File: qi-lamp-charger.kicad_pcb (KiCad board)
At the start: 2 copper layers, 41.5 x 44 mm, 85 parts, among them J1 Conn_01x03, J2 Conn_01x02, J4 Conn_01x06, J5 Conn_01x03, Q1 BSS308PE H6327, SW1 SKTDLDE010, U1 SLG5NV1430V, U2 BQ51050BRHL, U3 ESP-12E

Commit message: Shematic changed
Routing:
- net LED_V+: track 160.8 -> 159.8 mm
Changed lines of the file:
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@@
   (via (at 90.4 104.2) (size 0.8) (drill 0.4) (layers "F.Cu" "B.Cu") (net 5))
   (via (at 92.1 112) (size 0.8) (drill 0.4) (layers "F.Cu" "B.Cu") (net 5))
-  (via (at 96.3 105.5) (size 0.8) (drill 0.4) (layers "F.Cu" "B.Cu") (net 5))
+  (via (at 96.6 105.3) (size 0.8) (drill 0.4) (layers "F.Cu" "B.Cu") (net 5))
   (via (at 81.5 92.1) (size 0.8) (drill 0.4) (layers "F.Cu" "B.Cu") (net 5))
   (via (at 97.6 116.9) (size 0.8) (drill 0.4) (layers "F.Cu" "B.Cu") (net 5))
@@
   (segment (start 90.974999 110.3) (end 90.975 109.625) (width 0.35) (layer "B.Cu") (net 15))
   (segment (start 90.325 107.375) (end 90.3 107.35) (width 0.5) (layer "B.Cu") (net 15))
+  (segment (start 95.875489 107.224511) (end 95.5 107.6) (width 0.25) (layer "B.Cu") (net 15))
   (segment (start 81.4 103.1) (end 81.2 102.9) (width 0.25) (layer "B.Cu") (net 15))
   (segment (start 103.325 89.4) (end 103.125 89.6) (width 0.25) (layer "B.Cu") (net 15))
@@
   (segment (start 82.1 110.4) (end 81.4 109.7) (width 0.25) (layer "B.Cu") (net 15))
   (segment (start 88.1 109.2) (end 89.95 107.35) (width 0.5) (layer "B.Cu") (net 15))
+  (segment (start 98.85 101.05) (end 95.875489 104.024511) (width 0.25) (layer "B.Cu") (net 15))
   (segment (start 107.700978 110.2) (end 107.875 110.2) (width 0.25) (layer "B.Cu") (net 15))
   (segment (start 91.3 107.4) (end 91.325 107.375) (width 0.5) (layer "B.Cu") (net 15))
-  (segment (start 95.5 104.4) (end 95.5 105.9) (width 0.25) (layer "B.Cu") (net 15))
   (segment (start 103.2 105.4) (end 98.85 101.05) (width 0.25) (layer "B.Cu") (net 15))
   (segment (start 95.275 107.375) (end 95.5 107.6) (width 0.5) (layer "B.Cu") (net 15))
@@
   (segment (start 102.1 87) (end 102 86.9) (width 0.25) (layer "B.Cu") (net 15))
   (segment (start 104.5 89.4) (end 104.5 95.4) (width 0.25) (layer "B.Cu") (net 15))
-  (segment (start 98.85 101.05) (end 95.5 104.4) (width 0.25) (layer "B.Cu") (net 15))
+  (segment (start 95.875489 104.024511) (end 95.875489 107.224511) (width 0.25) (layer "B.Cu") (net 15))
   (segment (start 106.5 106.1) (end 105.8 105.4) (width 0.25) (layer "B.Cu") (net 15))
-  (segment (start 95.5 105.9) (end 95.5 107.6) (width 0.25) (layer "B.Cu") (net 15))
   (segment (start 112.870636 90.937083) (end 114.397432 90.937083) (width 0.25) (layer "F.Cu") (net 16))
   (segment (start 112.1 85.2) (end 112.1 90.166447) (width 0.25) (layer "F.Cu") (net 16))
@@
   (segment (start 106.4 104.375) (end 106.425 104.4) (width 0.5) (layer "F.Cu") (net 23))
   (segment (start 104.4 93.625) (end 104.625 93.625) (width 0.5) (layer "F.Cu") (net 23))
-  (segment (start 93.5 100) (end 94.8 101.3) (width 0.5) (layer "F.Cu") (net 23))
   (segment (start 112.111791 109.821762) (end 111.933553 110) (width 0.5) (layer "F.Cu") (net 23))
+  (segment (start 94.8 101.775) (end 97.6 104.575) (width 0.5) (layer "F.Cu") (net 23))
   (segment (start 110.698609 110) (end 106.425 105.726391) (width 0.5) (layer "F.Cu") (net 23))
   (segment (start 86.4 107.5) (end 85.438209 106.538209) (width 0.5) (layer "F.Cu") (net 23))
   (segment (start 106.4 104.375) (end 106.375 104.4) (width 0.5) (layer "F.Cu") (net 23))
   (segment (start 85.438209 106.538209) (end 85.438209 105.578238) (width 0.5) (layer "F.Cu") (net 23))
-  (segment (start 94.8 101.3) (end 94.8 103.5) (width 0.5) (layer "F.Cu") (net 23))
   (segment (start 99.925 104.575) (end 103.449999 101.050001) (width 0.5) (layer "F.Cu") (net 23))
-  (segment (start 93.6 97.55) (end 93.5 97.65) (width 0.5) (layer "F.Cu") (net 23))
   (segment (start 95.625 115.4) (end 95.5 115.525) (width 0.5) (layer "F.Cu") (net 23))
   (segment (start 83.859394 110.859394) (end 82.4 109.4) (width 0.5) (layer "F.Cu") (net 23))
@@
   (segment (start 87.888209 90.178238) (end 87.888209 89.270461) (width 0.5) (layer "F.Cu") (net 23))
   (segment (start 105 101.050001) (end 106.4 102.450001) (width 0.5) (layer "F.Cu") (net 23))
-  (segment (start 94.8 103.5) (end 95.875 104.575) (width 0.5) (layer "F.Cu") (net 23))
+  (segment (start 93.6 97.55) (end 93.5 97.65) (width 0.5) (layer "F.Cu") (net 23))
   (segment (start 97.55 104.625) (end 97.6 104.575) (width 0.5) (layer "F.Cu") (net 23))
   (segment (start 92.9 86.7) (end 94.5 88.3) (width 0.5) (layer "F.Cu") (net 23))
@@
   (segment (start 93.575 115.525) (end 95.5 115.525) (width 0.5) (layer "F.Cu") (net 23))
   (segment (start 91.6 86.7) (end 92.9 86.7) (width 0.5) (layer "F.Cu") (net 23))
+  (segment (start 93.5 100) (end 94.8 101.3) (width 0.5) (layer "F.Cu") (net 23))
   (segment (start 91.3 117.8) (end 93.575 115.525) (width 0.5) (layer "F.Cu") (net 23))
   (segment (start 88.55 116.4) (end 89.95 117.8) (width 0.5) (layer "F.Cu") (net 23))
+  (segment (start 93.5 97.65) (end 93.5 100) (width 0.5) (layer "F.Cu") (net 23))
   (segment (start 87.3 116) (end 83.859394 112.559394) (width 0.5) (layer "F.Cu") (net 23))
   (segment (start 90.0125 88.2875) (end 91.6 86.7) (width 0.5) (layer "F.Cu") (net 23))
@@
   (segment (start 95.475 115.525) (end 95.5 115.525) (width 0.5) (layer "F.Cu") (net 23))
   (segment (start 88.87117 88.2875) (end 90.0125 88.2875) (width 0.5) (layer "F.Cu") (net 23))
+  (segment (start 94.8 101.3) (end 94.8 101.775) (width 0.5) (layer "F.Cu") (net 23))
   (segment (start 102.45 84.6) (end 104.375 84.6) (width 0.5) (layer "F.Cu") (net 23))
   (segment (start 109.875 89.734971) (end 109.875 89.425) (width 0.25) (layer "F.Cu") (net 23))
   (segment (start 103.449999 101.050001) (end 105 101.050001) (width 0.5) (layer "F.Cu") (net 23))
-  (segment (start 93.5 97.65) (end 93.5 100) (width 0.5) (layer "F.Cu") (net 23))
-  (segment (start 95.875 104.575) (end 97.6 104.575) (width 0.5) (layer "F.Cu") (net 23))
   (segment (start 106.425 105.726391) (end 106.425 104.4) (width 0.5) (layer "F.Cu") (net 23))
   (segment (start 104.375 84.6) (end 104.4 84.625) (width 0.5) (layer "F.Cu") (net 23))
@@
   (segment (start 103.5 104.8) (end 108.2 104.8) (width 0.25) (layer "B.Cu") (net 48))
   (segment (start 89.2 97.334643) (end 89.2 97.8) (width 0.25) (layer "F.Cu") (net 49))
+  (segment (start 91.8 103.1) (end 91.8 103.2) (width 0.25) (layer "F.Cu") (net 49))
+  (segment (start 87 95.5) (end 87.365357 95.5) (width 0.25) (layer "F.Cu") (net 49))
   (segment (start 94 105.4) (end 94 109.1) (width 0.25) (layer "F.Cu") (net 49))
-  (segment (start 87 95.5) (end 87.365357 95.5) (width 0.25) (layer "F.Cu") (net 49))
   (segment (start 91.8 103.2) (end 94 105.4) (width 0.25) (layer "F.Cu") (net 49))
   (segment (start 87.365357 95.5) (end 89.2 97.334643) (width 0.25) (layer "F.Cu") (net 49))
@@
   (via (at 89.2 97.8) (size 0.8) (drill 0.4) (layers "F.Cu" "B.Cu") (net 49))
   (via (at 94 109.1) (size 0.8) (drill 0.4) (layers "F.Cu" "B.Cu") (net 49))
-  (via (at 91.8 103.2) (size 0.8) (drill 0.4) (layers "F.Cu" "B.Cu") (net 49))
+  (via (at 91.8 103.1) (size 0.8) (drill 0.4) (layers "F.Cu" "B.Cu") (net 49))
   (via (at 87 95.5) (size 0.8) (drill 0.4) (layers "F.Cu" "B.Cu") (net 49))
+  (segment (start 91.8 102.1) (end 92.9 101) (width 0.25) (layer "B.Cu") (net 49))
   (segment (start 95.2 96) (end 94.1 96) (width 0.25) (layer "B.Cu") (net 49))
   (segment (start 91.6 96) (end 91 96.6) (width 0.25) (layer "B.Cu") (net 49))
@@
   (segment (start 94 109.1) (end 94 111.5) (width 0.2) (layer "B.Cu") (net 49))
   (segment (start 94.1 96) (end 91.6 96) (width 0.25) (layer "B.Cu") (net 49))
+  (segment (start 92.9 101) (end 94 101) (width 0.25) (layer "B.Cu") (net 49))
   (segment (start 83.925001 95.5) (end 83.300002 96.124999) (width 0.25) (layer "B.Cu") (net 49))
   (segment (start 87 95.5) (end 83.925001 95.5) (width 0.25) (layer "B.Cu") (net 49))
@@
   (segment (start 96.6 97.4) (end 95.2 96) (width 0.25) (layer "B.Cu") (net 49))
   (segment (start 89.8 97.8) (end 89.2 97.8) (width 0.25) (layer "B.Cu") (net 49))
-  (segment (start 91.8 102.1) (end 92.9 101) (width 0.25) (layer "B.Cu") (net 49))
-  (segment (start 92.9 101) (end 94 101) (width 0.25) (layer "B.Cu") (net 49))
   (segment (start 91 96.6) (end 89.8 97.8) (width 0.25) (layer "B.Cu") (net 49))
   (segment (start 95.6 101) (end 97.9 98.7) (width 0.25) (layer "B.Cu") (net 49))
   (segment (start 95.05 112.55) (end 96.349998 112.55) (width 0.2) (layer "B.Cu") (net 49))
-  (segment (start 91.8 103.2) (end 91.8 102.1) (width 0.25) (layer "B.Cu") (net 49))
+  (segment (start 91.8 103.1) (end 91.8 102.1) (width 0.25) (layer "B.Cu") (net 49))
   (segment (start 95.6 98.6) (end 95.6 98.9) (width 0.25) (layer "F.Cu") (net 51))
   (segment (start 95.6 98.9) (end 98.9 102.2) (width 0.25) (layer "F.Cu") (net 51))

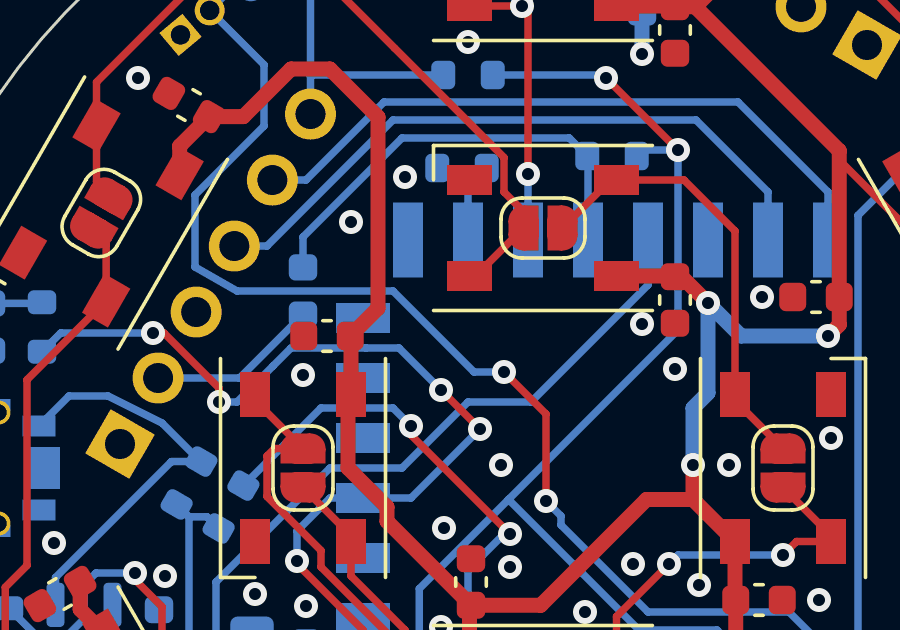
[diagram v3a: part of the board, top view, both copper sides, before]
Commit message: Minor corrections to layout (not up to date with previous commit)
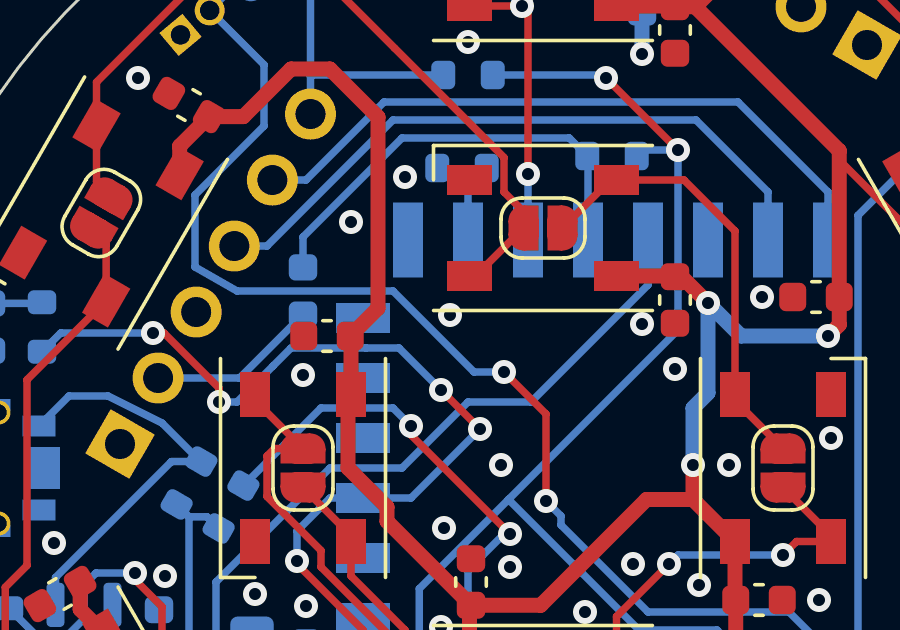
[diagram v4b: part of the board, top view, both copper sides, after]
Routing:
- net GND: vias 40 -> 41
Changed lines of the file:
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@@
   (via (at 90.4 104.2) (size 0.8) (drill 0.4) (layers "F.Cu" "B.Cu") (net 5))
   (via (at 92.1 112) (size 0.8) (drill 0.4) (layers "F.Cu" "B.Cu") (net 5))
+  (via (at 96.9 94.9) (size 0.8) (drill 0.4) (layers "F.Cu" "B.Cu") (net 5))
   (via (at 96.6 105.3) (size 0.8) (drill 0.4) (layers "F.Cu" "B.Cu") (net 5))
   (via (at 81.5 92.1) (size 0.8) (drill 0.4) (layers "F.Cu" "B.Cu") (net 5))

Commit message: Puzzle #6
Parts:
- removed H1, H2, H3: MountingHole, MountingHole:MountingHole_3.2mm_M3_ISO14580
- removed JP12: SolderJumper_2_Bridged, Jumper:SolderJumper-2_P1.3mm_Bridged_RoundedPad1.0x1.5mm
- added D13: CD0603-B0340R, Diode_SMD:D_0603_1608Metric, B.Cu at (64.2, 82.2)
- added R15: 20k, Resistor_SMD:R_0603_1608Metric, B.Cu at (56.1, 79.6)
- added R16: 20k, Resistor_SMD:R_0603_1608Metric, F.Cu at (82.5, 96.0)
- added R17: 340k, Resistor_SMD:R_0603_1608Metric, B.Cu at (60.1, 82.1)
- added R18: 100k, Resistor_SMD:R_0603_1608Metric, B.Cu at (56.1, 82.1)
- moved D12 31.4 mm to (64.2, 79.6), turned to 180 degrees
- moved TP1 0.89 mm to (88.7, 85.2), turned to 130 degrees
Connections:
- net PWR_ON/~{OFF} renamed KEEP_ALIVE
- D12 pad 1: DTR -> ~{Qi_CHG/LED}
- D12 pad 2: ESP_GPIO0 -> Net-(Q1-Pad1)
- Q1 pad 1: BTN -> Net-(Q1-Pad1)
- R11 pad 1: ESP_GPIO0 -> DTR
- R14 pad 1: BTN -> Net-(Q1-Pad1)
- R4 pad 1: ~{Qi_CHG/LED} -> Net-(R4-Pad1)
- SW1 pad 2: BTN -> ~{BTN}
- TP1 pad 2: ~{ESP_RST} -> DTR
- U2 pad 7: ~{Qi_CHG/LED} -> Net-(R4-Pad1)
- U3 pad 1: ~{ESP_RST} -> RTS
- U3 pad 18: ESP_GPIO0 -> DTR
- U3 pad 2: NTC -> BAT_ADC
- U3 pad 20: unconnected-(U3-Pad20) -> Qi_TS/CTRL
- U3 pad 5: BTN -> ~{BTN}
- U3 pad 7: Qi_TS/CTRL -> unconnected-(U3-Pad7)
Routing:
- net GND: track 38.0 -> 87.0 mm, vias 41 -> 48
- net ~{ESP_RST}: track 41.7 -> 0.00 mm, vias 2 -> 0
- net ~{Qi_CHG/LED}: track 38.6 -> 0.00 mm, vias 6 -> 0
- net RTS: track 9.98 -> 40.8 mm, vias 0 -> 2
- net ~{BTN}: track 0.00 -> 29.4 mm, vias 0 -> 4
- net DTR: track 5.71 -> 32.3 mm, vias 0 -> 1
- net Net-(R4-Pad1): track 0.00 -> 25.1 mm, vias 0 -> 2
- net ESP_GPIO0: track 14.9 -> 0.00 mm
- net BAT_ADC: track 0.00 -> 14.8 mm, vias 0 -> 1
- net BTN: track 13.9 -> 0.00 mm
- net Net-(Q1-Pad1): track 0.00 -> 7.38 mm
- net NTC: track 40.0 -> 33.0 mm
- net LED_DOUT: track 22.4 -> 18.7 mm
- net Qi_TS/CTRL: track 45.4 -> 49.0 mm, vias 2 -> 3
- net +VSW: track 77.9 -> 79.5 mm
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
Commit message: Puzzle #7
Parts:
- moved R15 33.6 mm to (88.5, 88.5), turned to 135 degrees
- moved R18 29.7 mm to (85.2, 88.0), turned to -130 degrees
- moved R17 25.3 mm to (83.3, 92.3), turned to -90 degrees
- moved D12 25.3 mm to (87.4, 89.6), turned to 135 degrees
- moved D13 23.7 mm to (86.0, 91.5), turned to 0 degrees
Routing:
- net GND: track 87.0 -> 239.0 mm, vias 48 -> 52
- net BAT_ADC: track 14.8 -> 47.5 mm, vias 1 -> 2
- net ~{Qi_CHG/LED}: track 0.00 -> 18.6 mm, vias 0 -> 2
- net Net-(D12-Pad2): track 7.38 -> 18.9 mm
- net Net-(R15-Pad2): track 25.1 -> 35.1 mm
- net ~{BTN}: track 29.4 -> 36.4 mm, vias 4 -> 5
- net +VSW: track 79.5 -> 84.8 mm
- net DTR: track 32.3 -> 33.4 mm
- net LED_V+: track 160.8 -> 159.7 mm

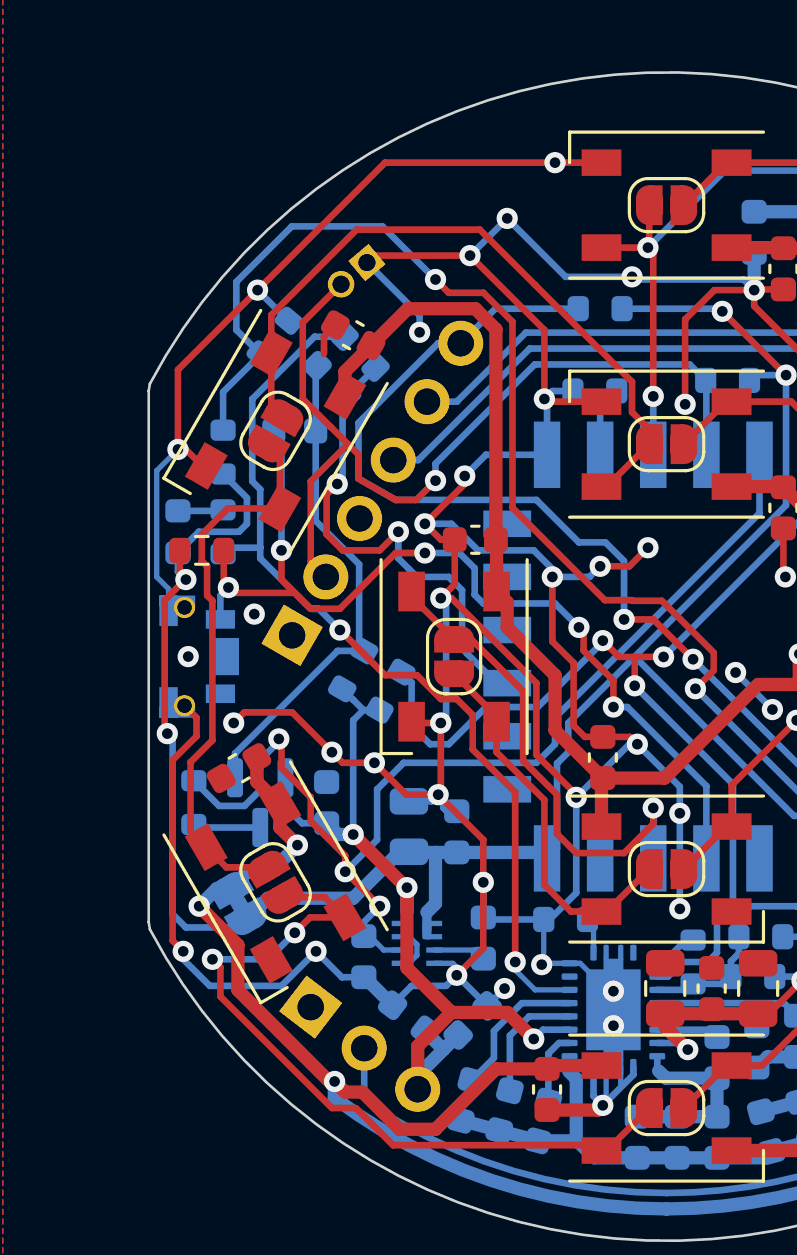
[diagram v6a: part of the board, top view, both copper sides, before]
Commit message: Puzzle complete incl. DRC
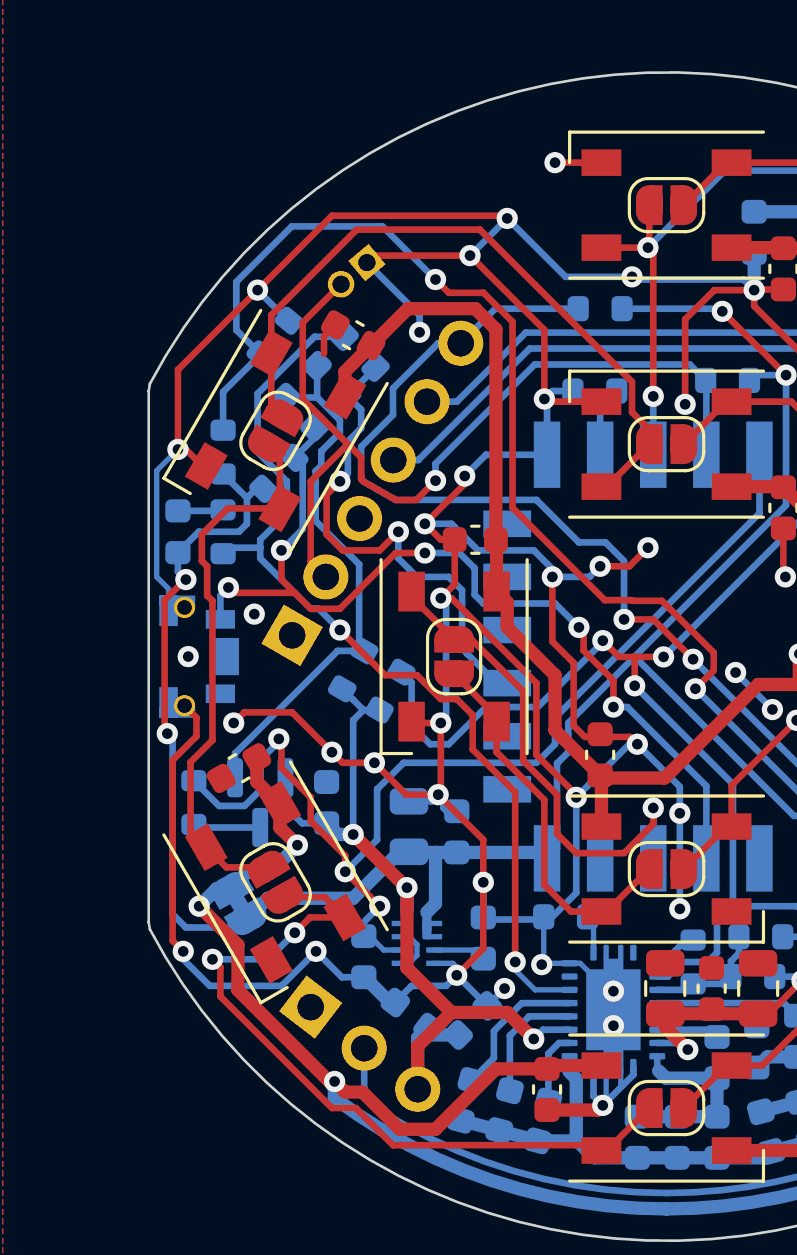
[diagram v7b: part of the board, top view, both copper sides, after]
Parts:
- R16: moved to B.Cu
- moved R16 4.10 mm to (85.4, 93.1), turned to -135 degrees
- moved D13 0.73 mm to (86.2, 90.8), turned to 135 degrees
- moved C4 0.14 mm to (90.4, 113.5)
- moved C32 0.14 mm to (97.5, 103.7)
- moved R5 0.10 mm to (96.2, 109.8)
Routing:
- net GND: track 239.0 -> 236.4 mm
- net Net-(D12-Pad2): track 18.9 -> 20.8 mm
- net ~{BTN}: track 36.4 -> 35.7 mm
- net Net-(R15-Pad2): track 35.1 -> 35.8 mm

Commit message: As ordered
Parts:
- added H1: MountingHole, MountingHole:MountingHole_2.2mm_M2, F.Cu at (93.0, 81.0)
- added H2: MountingHole, MountingHole:MountingHole_2.2mm_M2, F.Cu at (120.0, 100.0)
- D11: value LED_Green -> LED_Red
- Q1: value BSS308PE H6327 -> BSS 209PW
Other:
- board text added: "Qi WiFi Lamp r${REVISION} Step7.dk Martin Axelsen"
- board text removed: "r${REVISION} Qi WiFi Lamp Step7.dk Martin Axelsen"
